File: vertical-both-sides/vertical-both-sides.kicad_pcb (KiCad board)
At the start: 2 copper layers, 5.1 x 15.3 mm, 3 parts, among them J1 Grove-I2C-connector, J2 Conn_01x02, J3 Conn_01x02

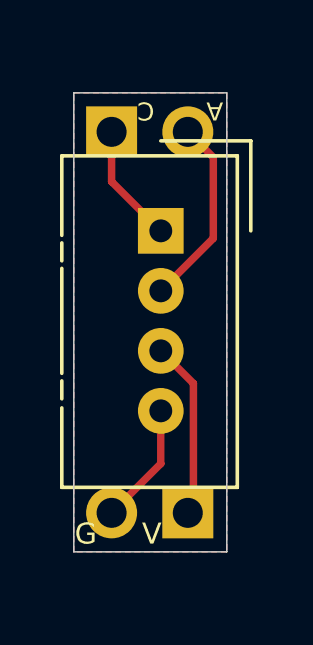
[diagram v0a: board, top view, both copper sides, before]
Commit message: Update silk lines for rev2021.02
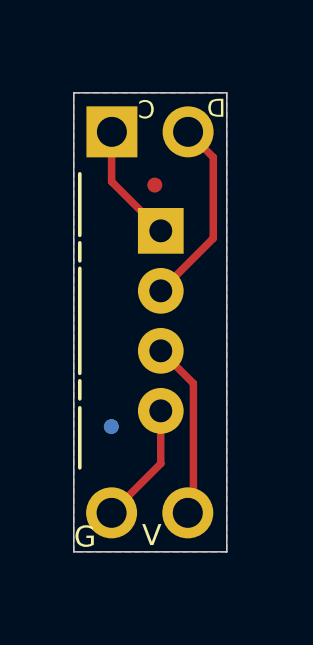
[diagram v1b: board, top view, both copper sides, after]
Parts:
- added Fid1: Fiducial_0.5mm_Mask1mm, Fiducial:Fiducial_0.5mm_Mask1mm, F.Cu at (149.0, 82.9)
- added Fid2: Fiducial_0.5mm_Mask1mm, Fiducial:Fiducial_0.5mm_Mask1mm, B.Cu at (147.6, 90.9)
- J1: footprint Connector:NS-Tech_Grove_1x04_P2mm_Vertical -> my-kicad-footprints:NS-Tech_Grove_1x04_P2mm_Vertical_silk_inside
- J2: footprint Connector_PinHeader_2.54mm:PinHeader_1x02_P2.54mm_Vertical -> my-kicad-footprints:PinHeader_1x02_P2.54mm_Vertical_silk_inside
- J3: footprint Connector_PinHeader_2.54mm:PinHeader_1x02_P2.54mm_Vertical -> my-kicad-footprints:PinHeader_1x02_P2.54mm_Vertical_all_circle_silk_inside
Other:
- board text added: "D"
- board text added: "Rev2021.02"
- board text removed: "A"
- board text removed: "Rev2020.12"

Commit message: Update revision for bertical botn and one line and horizontal both
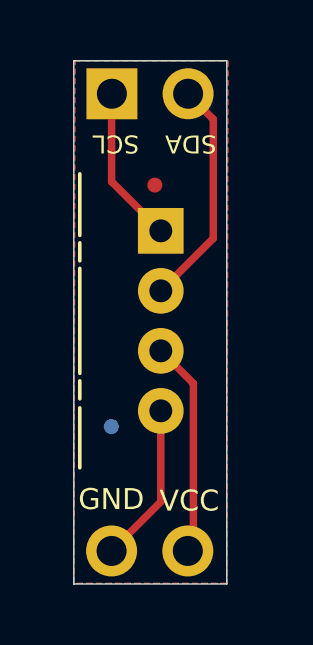
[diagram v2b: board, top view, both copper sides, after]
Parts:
- moved J2 1.27 mm to (147.6, 79.8)
- moved J3 1.27 mm to (150.1, 95.1)
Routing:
- net Net-(J1-Pad1): track 3.98 -> 5.25 mm
- net Net-(J1-Pad2): track 6.38 -> 7.65 mm
- net GND: track 4.08 -> 5.35 mm
- net Net-(J1-Pad3): track 5.93 -> 7.20 mm
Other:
- board size 5.1 x 15.3 mm -> 5.1 x 17.4 mm
- board text added: "GND"
- board text added: "Rev2021.04"
- board text added: "SCL"
- board text added: "SDA"
- board text added: "VCC"
- board text removed: "C"
- board text removed: "D"
- board text removed: "G"
- board text removed: "Rev2021.02"
- board text removed: "V"
